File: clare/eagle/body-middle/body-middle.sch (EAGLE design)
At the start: 10 parts

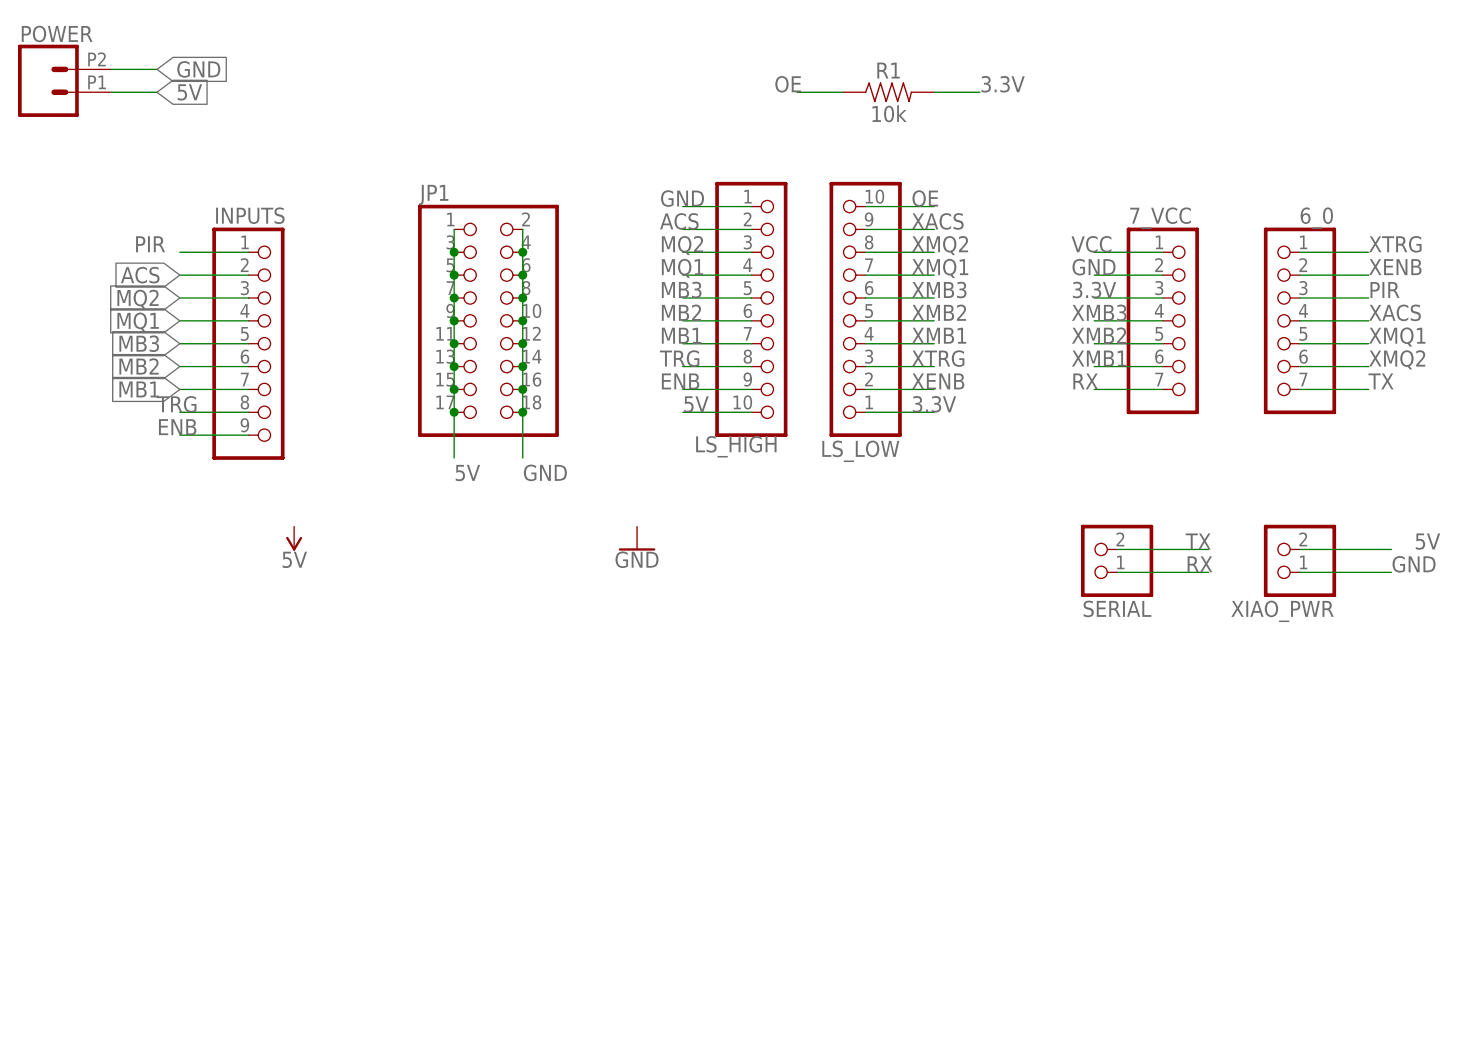
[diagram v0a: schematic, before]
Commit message: New arduino nano pcb for body middle with working code
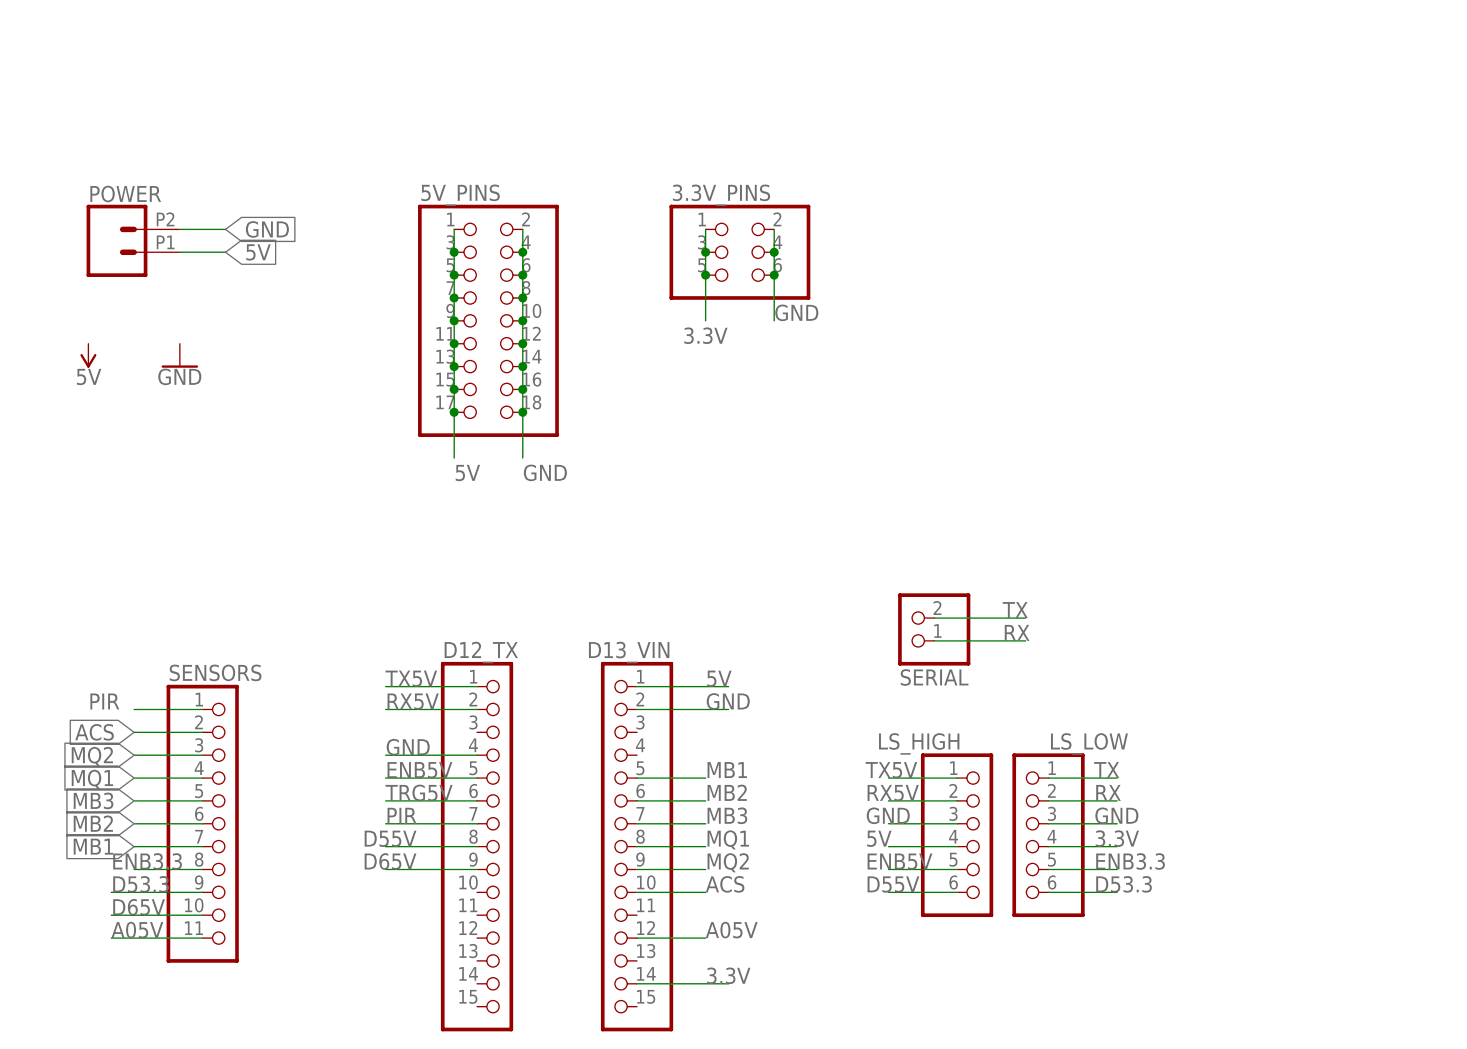
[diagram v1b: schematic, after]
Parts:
- removed 6_0, 7_VCC: (no value), pinhead:PINHD-1X7
- removed INPUTS: (no value), pinhead:PINHD-1X9
- removed R1: 10k, SparkFun-Resistors:10KOHM-HORIZ-1/4W-1%
- removed XIAO_PWR: (no value), pinhead:PINHD-1X2
- added 3.3V_PINS: (no value), pinhead:PINHD-2X3
- added D12_TX, D13_VIN: (no value), pinhead:PINHD-1X15
- added SENSORS: (no value), pinhead:PINHD-1X11
- LS_HIGH, LS_LOW: device pinhead:PINHD-1X10 -> pinhead:PINHD-1X6
- renumbered JP1 to 5V_PINS
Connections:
- removed net ENB: INPUTS.9, LS_HIGH.9
- removed net OE: LS_LOW.10, R1.1
- removed net TRG: INPUTS.8, LS_HIGH.8
- removed net VCC: 7_VCC.1
- removed net XACS: 6_0.4, LS_LOW.9
- removed net XENB: 6_0.2, LS_LOW.2
- removed net XMB1: 7_VCC.6, LS_LOW.4
- removed net XMB2: 7_VCC.5, LS_LOW.5
- removed net XMB3: 7_VCC.4, LS_LOW.6
- removed net XMQ1: 6_0.5, LS_LOW.7
- removed net XMQ2: 6_0.6, LS_LOW.8
- removed net XTRG: 6_0.1, LS_LOW.3
- new net A05V: D13_VIN.12, SENSORS.11
- new net D53.3: LS_LOW.6, SENSORS.9
- new net D55V: D12_TX.8, LS_HIGH.6
- new net D65V: D12_TX.9, SENSORS.10
- new net ENB3.3: LS_LOW.5, SENSORS.8
- new net ENB5V: D12_TX.5, LS_HIGH.5
- new net RX5V: D12_TX.2, LS_HIGH.2
- new net TRG5V: D12_TX.6
- new net TX5V: D12_TX.1, LS_HIGH.1
- net 3.3V: now also 3.3V_PINS.1, 3.3V_PINS.3, 3.3V_PINS.5, D13_VIN.14, LS_LOW.4; no longer 7_VCC.3, LS_LOW.1, R1.2
- net 5V: now also D13_VIN.1, LS_HIGH.4; no longer LS_HIGH.10, XIAO_PWR.2
- net ACS: now also D13_VIN.10, SENSORS.2; no longer INPUTS.2, LS_HIGH.2
- net GND: now also 3.3V_PINS.2, 3.3V_PINS.4, 3.3V_PINS.6, D12_TX.4, D13_VIN.2, LS_HIGH.3, LS_LOW.3; no longer 7_VCC.2, LS_HIGH.1, XIAO_PWR.1
- net MB1: now also D13_VIN.5, SENSORS.7; no longer INPUTS.7, LS_HIGH.7
- net MB2: now also D13_VIN.6, SENSORS.6; no longer INPUTS.6, LS_HIGH.6
- net MB3: now also D13_VIN.7, SENSORS.5; no longer INPUTS.5, LS_HIGH.5
- net MQ1: now also D13_VIN.8, SENSORS.4; no longer INPUTS.4, LS_HIGH.4
- net MQ2: now also D13_VIN.9, SENSORS.3; no longer INPUTS.3, LS_HIGH.3
- net PIR: now also D12_TX.7, SENSORS.1; no longer 6_0.3, INPUTS.1
- net RX: now also LS_LOW.2; no longer 7_VCC.7
- net TX: now also LS_LOW.1; no longer 6_0.7
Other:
- moved on the sheet: POWER, SERIAL
